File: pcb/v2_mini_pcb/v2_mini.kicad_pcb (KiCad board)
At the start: 6 copper layers, 70.8 x 36 mm, 109 parts, among them J1 Conn_Coaxial, J2 GTFP08441BEU, J3 SFV24R-2STE1HLF, J5 TC2030, J6 USB4105-GF-A, Q1 NTNS3164NZT5G, SW1 SW_Push, SW2 SW_Push, SW3 SW_Push, SW4 SW_Push, SW5 SW_Push, SW6 SW_Push, U1 UM980, U10 TPS63802DLAR, U3 SCH16T-K01-1, U4 LP5813ADRRR, U5 TCA9536ADTMR, U6 TPD4EUSB30, U8 BQ25622ERYKR, U9 MAX17048G_T10

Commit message: mcu routing done
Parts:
- R18, TP1, TP2: moved to B.Cu
- moved C12 70.1 mm to (123.5, 113.0)
- moved C24 66.1 mm to (120.7, 107.5), turned to 180 degrees
- moved R30 64.3 mm to (122.7, 107.5), turned to 180 degrees
- moved R18 64.3 mm to (121.3, 102.5), turned to 90 degrees
- moved R31 64.2 mm to (121.5, 113.0)
- moved TP2 53.2 mm to (121.8, 100.5), turned to 180 degrees
- moved TP1 53.2 mm to (121.8, 97.9), turned to 180 degrees
- moved J5 51.5 mm to (122.1, 110.2), turned to 180 degrees
- moved R8 34.6 mm to (86.3, 102.8), turned to 90 degrees
- moved R9 34.3 mm to (85.3, 106.0), turned to -90 degrees
- moved C10 24.3 mm to (89.0, 102.7), turned to -90 degrees
- moved C9 23.2 mm to (87.3, 104.4), turned to 90 degrees
- moved C11 23.1 mm to (85.3, 104.1), turned to 90 degrees
- moved SW1 0.60 mm to (82.3, 104.4), turned to 0 degrees
- moved SW2 0.58 mm to (82.3, 108.7)
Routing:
- net Net-(U2-GPIO34): track 0.00 -> 69.2 mm, vias 0 -> 2
- net Net-(U2-GPIO33): track 0.00 -> 64.2 mm, vias 0 -> 2
- net Net-(U2-GPIO61): track 0.00 -> 26.7 mm, vias 0 -> 1
- net Net-(U2-UART0_RXD/GPIO59): track 0.00 -> 23.0 mm
- net Net-(U2-UART0_TXD/GPIO58): track 0.00 -> 16.7 mm
- net Net-(U2-EN): track 0.00 -> 4.70 mm, vias 0 -> 3
- net +3V3: track 114.5 -> 118.9 mm, vias 15 -> 21
- net /ESP32-S31 MCU/JTAG_DP: track 0.00 -> 3.51 mm
- net /ESP32-S31 MCU/JTAG_DN: track 0.00 -> 2.97 mm
- net Net-(R18-Pad2): track 0.00 -> 1.74 mm
- net GND: vias 178 -> 194
- added copper zone on In2.Cu, net +3V3

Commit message: switches done
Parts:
- U5: moved to B.Cu
- moved C29 56.1 mm to (121.8, 104.8), turned to -90 degrees
- moved L2 3.66 mm to (131.4, 104.7)
- moved U5 0.45 mm to (122.3, 105.8), turned to 180 degrees
- turned SW6 to -90 degrees
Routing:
- net /ESP32-S31 MCU/POW_SDA: track 20.0 -> 60.8 mm, vias 3 -> 4
- net /ESP32-S31 MCU/POW_SCL: track 23.7 -> 62.4 mm, vias 2 -> 4
- net Net-(U5-P0): track 0.00 -> 12.5 mm
- net Net-(U5-P1): track 0.00 -> 8.09 mm
- net +3V3: track 118.9 -> 126.4 mm, vias 21 -> 23
- net Net-(U5-P2): track 0.00 -> 6.48 mm
- net Net-(U5-P3/INT): track 0.00 -> 2.43 mm
- net GND: vias 194 -> 200

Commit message: finish led layout
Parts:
- C27, C28: moved to B.Cu
- moved C27 61.6 mm to (125.2, 83.6), turned to 180 degrees
- moved C28 33.6 mm to (118.5, 84.8), turned to 90 degrees
- moved L2 21.8 mm to (121.7, 85.2), turned to 0 degrees
- moved D35 17.8 mm to (134.4, 81.6)
- moved D32 15.3 mm to (118.4, 81.5)
- moved U4 9.58 mm to (121.7, 82.0), turned to 0 degrees
- moved D34 7.74 mm to (129.8, 81.6)
- moved D33 2.86 mm to (124.9, 81.5)
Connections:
- U2 pad 14: /ESP32-S31 MCU/LED_EN -> unconnected-(U2-GPIO8-Pad14)
- U2 pad 50: unconnected-(U2-GPIO39-Pad50) -> /ESP32-S31 MCU/LED_EN
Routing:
- net /ESP32-S31 MCU/POW_SDA: track 60.8 -> 103.9 mm, vias 4 -> 6
- net /ESP32-S31 MCU/POW_SCL: track 62.4 -> 103.3 mm, vias 4 -> 5
- net Net-(D32-G_K): track 0.00 -> 31.0 mm, vias 0 -> 2
- net Net-(D32-R_K): track 0.00 -> 21.8 mm
- net /ESP32-S31 MCU/LED_EN: track 0.00 -> 21.4 mm, vias 0 -> 2
- net Net-(D32-B_K): track 0.00 -> 21.4 mm, vias 0 -> 2
- net Net-(D32-B_A): track 0.00 -> 18.8 mm, vias 0 -> 5
- net +3V3: track 126.4 -> 130.9 mm, vias 23 -> 24
- net Net-(U4-VOUT): track 0.00 -> 2.17 mm
- net GND: track 47.1 -> 49.2 mm, vias 200 -> 203
- net Net-(U4-SW): track 0.00 -> 2.03 mm

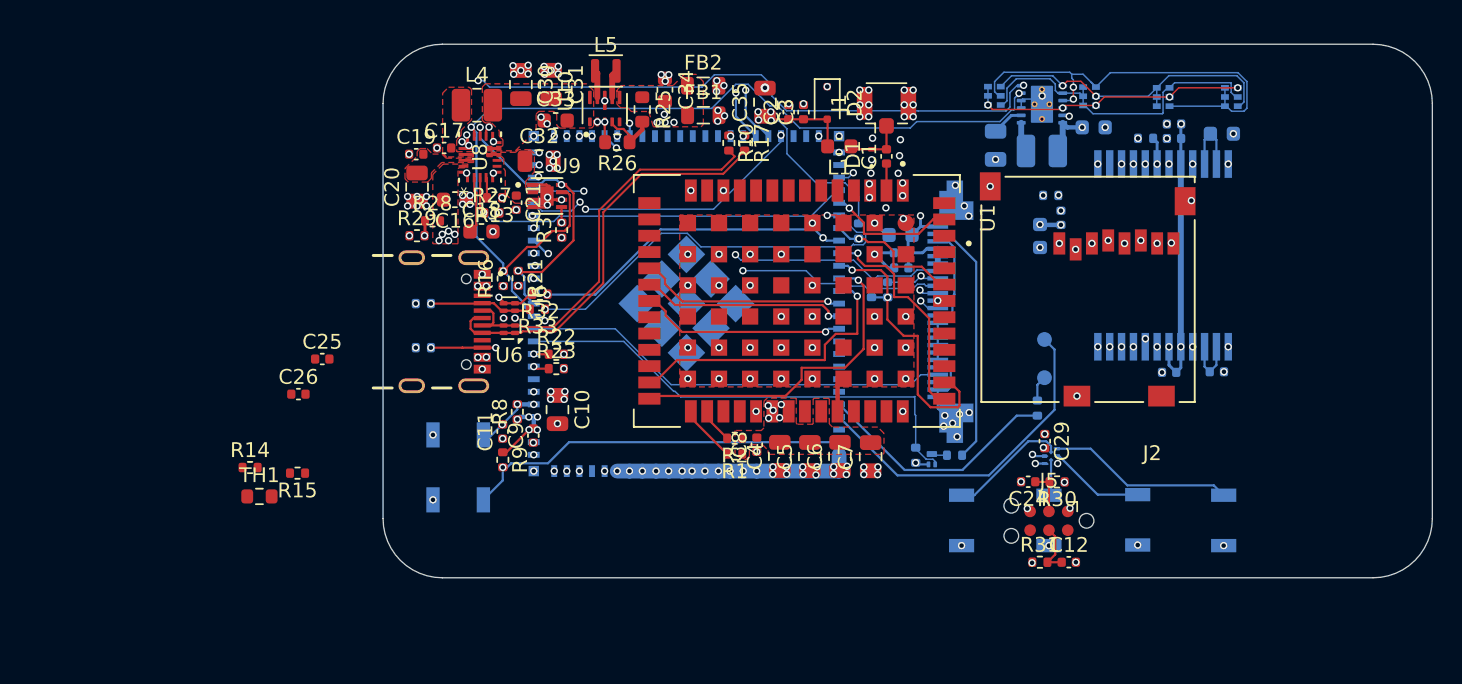
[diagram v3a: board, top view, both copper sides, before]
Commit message: nice outline cut
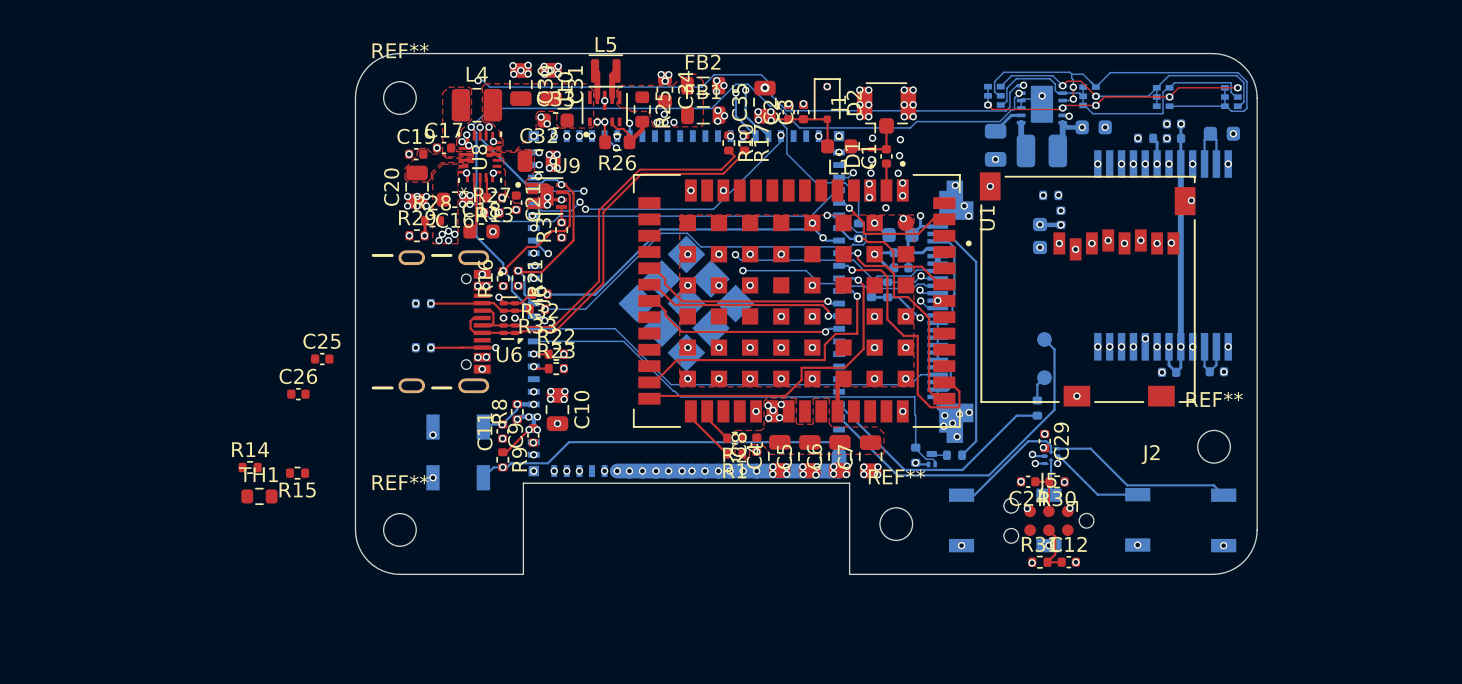
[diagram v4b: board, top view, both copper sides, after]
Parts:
- added REF**: MountingHole_2.2mm_M2, MountingHole:MountingHole_2.2mm_M2, F.Cu at (133.3, 105.2)
- added REF**: MountingHole_2.2mm_M2, MountingHole:MountingHole_2.2mm_M2, F.Cu at (78.3, 81.6)
- added REF**: MountingHole_2.2mm_M2, MountingHole:MountingHole_2.2mm_M2, F.Cu at (78.3, 110.8)
- added REF**: MountingHole_2.2mm_M2, MountingHole:MountingHole_2.2mm_M2, F.Cu at (111.8, 110.4)
- moved SW2 1.49 mm to (82.3, 107.2)
- moved SW1 0.53 mm to (82.3, 103.8)
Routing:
- net +3V3: track 130.9 -> 140.1 mm
- net Net-(U2-GPIO61): track 26.7 -> 25.0 mm
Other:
- board size 70.8 x 36 mm -> 60.8 x 35.1 mm

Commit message: fix last erc errors
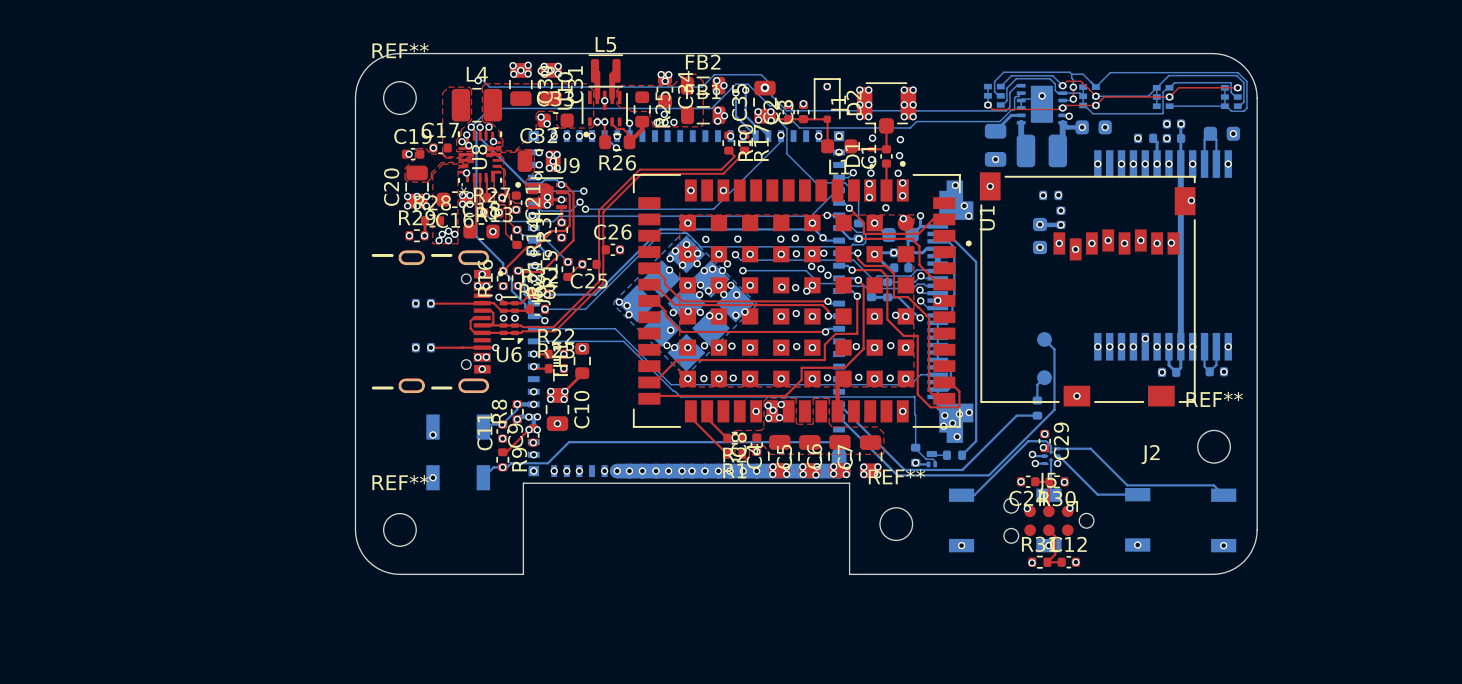
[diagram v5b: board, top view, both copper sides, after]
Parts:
- moved R14 23.8 mm to (86.2, 91.0), turned to -90 degrees
- moved TH1 23.6 mm to (90.6, 99.4), turned to 90 degrees
- moved C26 23.3 mm to (92.7, 91.9)
- moved R15 22.9 mm to (89.7, 93.2), turned to 90 degrees
- moved C25 19.1 mm to (91.1, 92.8), turned to 180 degrees
- moved C17 0.24 mm to (81.1, 85.0)
- moved C19 0.21 mm to (79.2, 85.4)
- turned R32 to 0 degrees
- turned R33 to 0 degrees
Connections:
- J6 pad A5: /ESP32-S31 MCU/USB_CC1 -> /Power + USB/USB_CC1_pre
- J6 pad B5: /ESP32-S31 MCU/USB_CC2 -> /Power + USB/USB_CC2_pre
- R11 pad 2: /ESP32-S31 MCU/USB_CC1 -> /Power + USB/USB_CC1_pre
- R12 pad 2: /ESP32-S31 MCU/USB_CC2 -> /Power + USB/USB_CC2_pre
- R32 pad 1: /ESP32-S31 MCU/USB_CC2 -> /Power + USB/USB_CC2_pre
- R33 pad 1: /ESP32-S31 MCU/USB_CC1 -> /Power + USB/USB_CC1_pre
- U6 pad 4: /ESP32-S31 MCU/USB_CC1 -> /Power + USB/USB_CC1_pre
- U6 pad 5: /ESP32-S31 MCU/USB_CC2 -> /Power + USB/USB_CC2_pre
- U6 pad 6: /ESP32-S31 MCU/USB_CC2 -> /Power + USB/USB_CC2_pre
- U6 pad 7: /ESP32-S31 MCU/USB_CC1 -> /Power + USB/USB_CC1_pre
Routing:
- net Net-(U8-TS): track 0.00 -> 15.6 mm, vias 0 -> 3
- net /Power + USB/USB_CC2_pre: track 0.00 -> 10.6 mm, vias 0 -> 3
- net /ESP32-S31 MCU/USB_CC2: track 32.5 -> 21.9 mm, vias 5 -> 2
- net /Power + USB/USB_CC1_pre: track 0.00 -> 6.94 mm, vias 0 -> 1
- net /ESP32-S31 MCU/USB_CC1: track 35.7 -> 28.7 mm, vias 3 -> 2
- net Net-(U8-TS_BIAS): track 0.00 -> 5.82 mm, vias 1 -> 0
- net GND: track 49.2 -> 52.3 mm, vias 203 -> 263
- net +3V3: track 140.1 -> 140.6 mm
- net /ESP32-S31 MCU/POW_SDA: vias 6 -> 5
- net /ESP32-S31 MCU/POW_SCL: vias 5 -> 4
- added copper zone on B.Cu, net GND

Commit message: move jtag
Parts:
- removed REF** (x4): MountingHole_2.2mm_M2, MountingHole:MountingHole_2.2mm_M2
- added H4: MountingHole_Pad, MountingHole:MountingHole_2.2mm_M2_Pad, F.Cu at (78.3, 110.8)
- added H5: MountingHole_Pad, MountingHole:MountingHole_2.2mm_M2_Pad, F.Cu at (111.8, 110.4)
- added H6: MountingHole_Pad, MountingHole:MountingHole_2.2mm_M2_Pad, F.Cu at (133.3, 105.2)
- added H7: MountingHole_Pad, MountingHole:MountingHole_2.2mm_M2_Pad, F.Cu at (78.3, 81.6)
- moved R31 8.25 mm to (127.7, 107.5), turned to 180 degrees
- moved J5 7.26 mm to (127.2, 104.9)
- moved C12 5.93 mm to (125.7, 107.5), turned to 180 degrees
- moved R30 3.78 mm to (123.0, 103.8), turned to -90 degrees
- moved C24 2.85 mm to (122.9, 105.7), turned to -90 degrees
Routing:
- net GND: track 52.3 -> 95.0 mm, vias 263 -> 256
- net Net-(U2-GPIO34): track 69.2 -> 60.2 mm
- net +3V3: track 140.6 -> 143.7 mm, vias 24 -> 23
- net /ESP32-S31 MCU/JTAG_DN: track 2.97 -> 5.64 mm
- net /ESP32-S31 MCU/JTAG_DP: track 3.51 -> 2.90 mm
- net Net-(U2-GPIO33): track 64.2 -> 63.6 mm

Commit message: draw
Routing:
- net +3V3: track 143.7 -> 56.9 mm, vias 23 -> 25
- net /ESP32-S31 MCU/POW_SCL: track 103.3 -> 102.6 mm
- added copper zone on In3.Cu, net GND
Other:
- outline, holes or cut-outs redrawn
- board text added: "gh/teehee567"

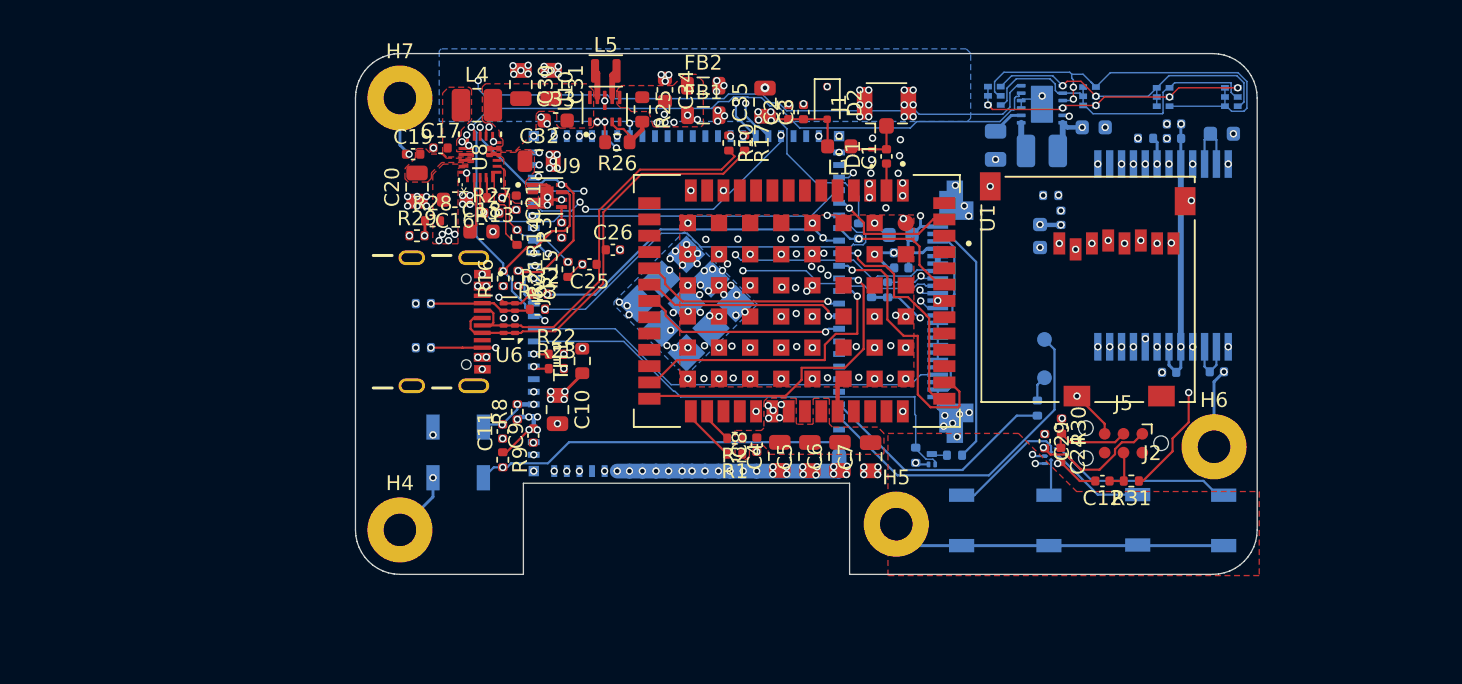
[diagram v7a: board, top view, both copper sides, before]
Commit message: fix drc problems nad d+d- and sd
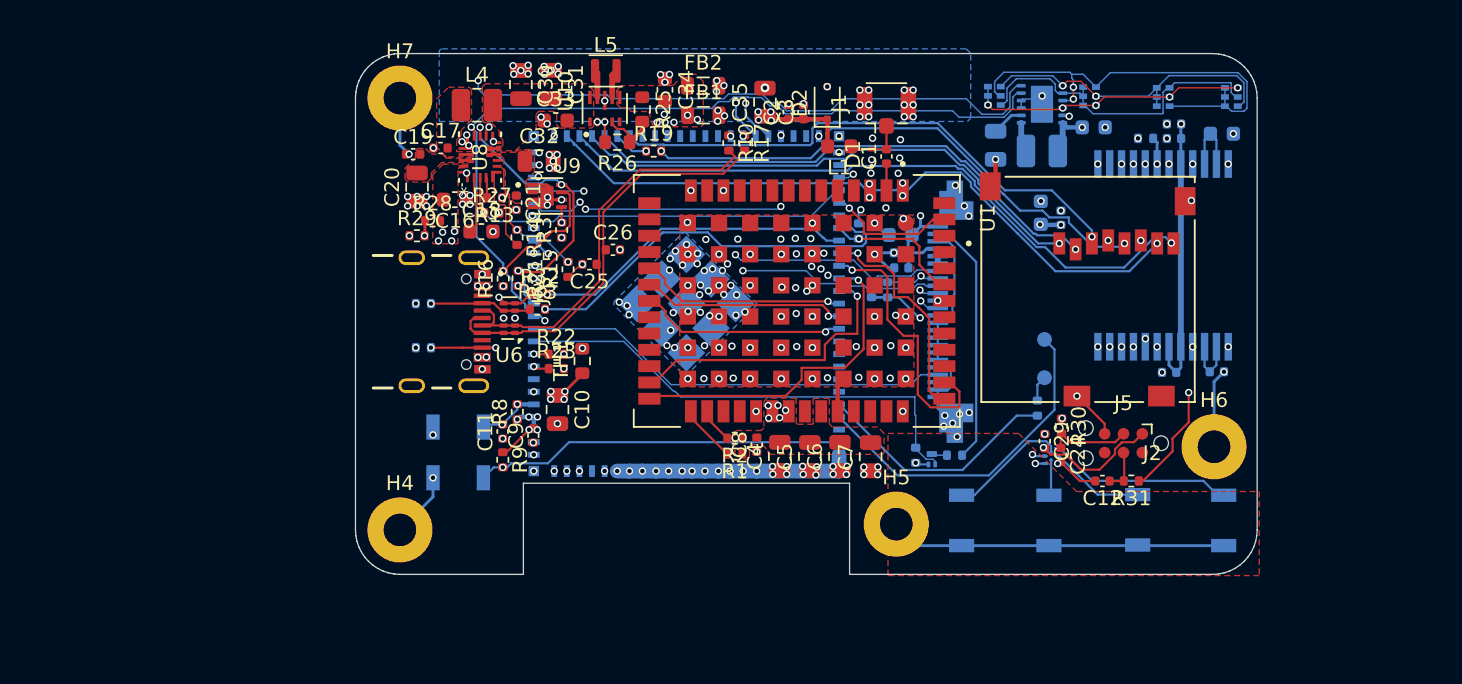
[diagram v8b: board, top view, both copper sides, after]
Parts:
- R19: moved to F.Cu
- moved R19 27.0 mm to (95.5, 85.2)
- moved C14 1.57 mm to (121.6, 89.4), turned to -90 degrees
- turned D2 to 90 degrees
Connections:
- C25 pad 1: /ESP32-S31 MCU/USB_DN -> /ESP32-S31 MCU/USB_DP
- C26 pad 1: /ESP32-S31 MCU/USB_DP -> /ESP32-S31 MCU/USB_DN
- D2 pad 1: GND -> +3V3_GNSS
- D2 pad 2: +3V3_GNSS -> GND
- J6 pad A6: /ESP32-S31 MCU/USB_DP -> /ESP32-S31 MCU/USB_DN
- J6 pad A7: /ESP32-S31 MCU/USB_DN -> /ESP32-S31 MCU/USB_DP
- J6 pad B6: /ESP32-S31 MCU/USB_DP -> /ESP32-S31 MCU/USB_DN
- J6 pad B7: /ESP32-S31 MCU/USB_DN -> /ESP32-S31 MCU/USB_DP
- R10 pad 2: /ESP32-S31 MCU/USB_DN -> /ESP32-S31 MCU/USB_DP
- R17 pad 2: /ESP32-S31 MCU/USB_DP -> /ESP32-S31 MCU/USB_DN
- U6 pad 1: /ESP32-S31 MCU/USB_DP -> /ESP32-S31 MCU/USB_DN
- U6 pad 10: /ESP32-S31 MCU/USB_DP -> /ESP32-S31 MCU/USB_DN
- U6 pad 2: /ESP32-S31 MCU/USB_DN -> /ESP32-S31 MCU/USB_DP
- U6 pad 9: /ESP32-S31 MCU/USB_DN -> /ESP32-S31 MCU/USB_DP
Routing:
- net Net-(J2-CLK): track 6.18 -> 36.3 mm
- net /ESP32-S31 MCU/SD_CLK: track 31.0 -> 2.37 mm, vias 2 -> 1
- net /ESP32-S31 MCU/USB_VBUS_S: track 28.4 -> 31.4 mm, vias 3 -> 4
- net +3V3_GNSS: track 41.0 -> 38.2 mm, vias 12 -> 13
- net GND: track 95.0 -> 96.9 mm, vias 256 -> 255
- net /ESP32-S31 MCU/USB_CC1: track 28.7 -> 27.2 mm, vias 2 -> 1
- net /ESP32-S31 MCU/SD_D1: track 43.6 -> 45.1 mm, vias 2 -> 1
- net /ESP32-S31 MCU/SD_D3: track 35.0 -> 36.0 mm, vias 2 -> 1
- net /ESP32-S31 MCU/SD_D2: track 34.8 -> 35.6 mm, vias 2 -> 1
- net /ESP32-S31 MCU/POW_SDA: track 103.6 -> 104.2 mm
- net /ESP32-S31 MCU/USB_DN: track 27.5 -> 28.2 mm
- net /ESP32-S31 MCU/SD_D0: track 46.1 -> 45.6 mm, vias 2 -> 1
- net /ESP32-S31 MCU/USB_CC2: track 21.9 -> 22.0 mm, vias 2 -> 1
- net /ESP32-S31 MCU/SD_CMD: track 36.1 -> 36.0 mm, vias 2 -> 1
- net Net-(U2-EN): vias 3 -> 2
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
